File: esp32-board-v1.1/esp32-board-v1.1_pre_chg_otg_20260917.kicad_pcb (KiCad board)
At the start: 4 copper layers, 55 x 84 mm, 110 parts, among them J1 USB_C_Receptacle_GCT_USB4105-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, J2 X05B20U24T, J3 microSD_DM3AT-SF-PEJM5_EPDF, J4 Molex_PicoBlade_53261-0271_1x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, J5 Molex_PicoBlade_53261-0271_1x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, Q1 SOT-323_SC-70, SW1 SW_SPST_B3U-1000P, SW2 SW_SPST_B3U-1000P, SW3 SW_SPST_B3U-1000P, SW4 SW_SPST_B3U-1000P, SW5 SW_SPST_B3U-1000P, U1 ESP32-S3-WROOM-1_EPDF, U2 Texas_RTW_WQFN-24-1EP_4x4mm_P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, U3 RNM0015A, U4 TDFN-8-1EP_2x2mm_P0.5mm_EP0.8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, U5 Texas_X2QFN-12_1.6x1.6mm_P0.4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, U6 SOT-23-6

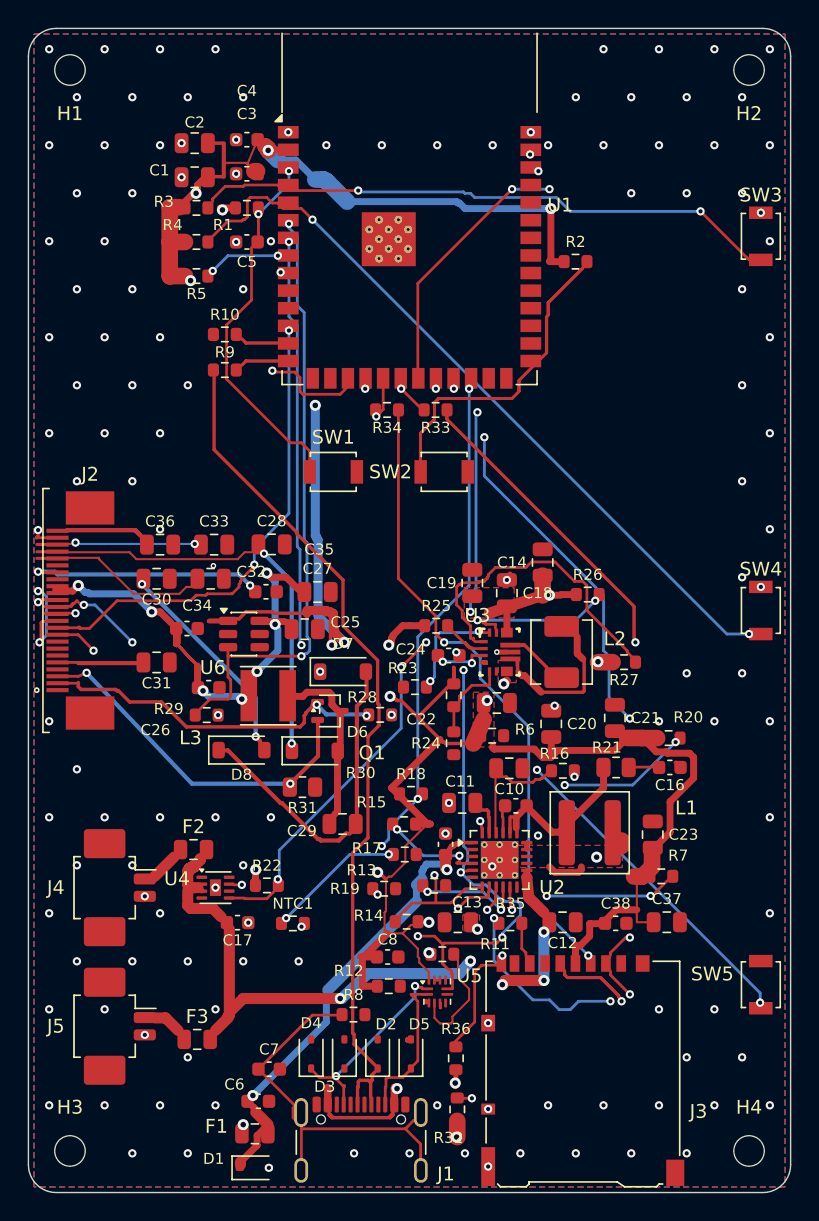
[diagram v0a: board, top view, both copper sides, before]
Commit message: 第四轮布线
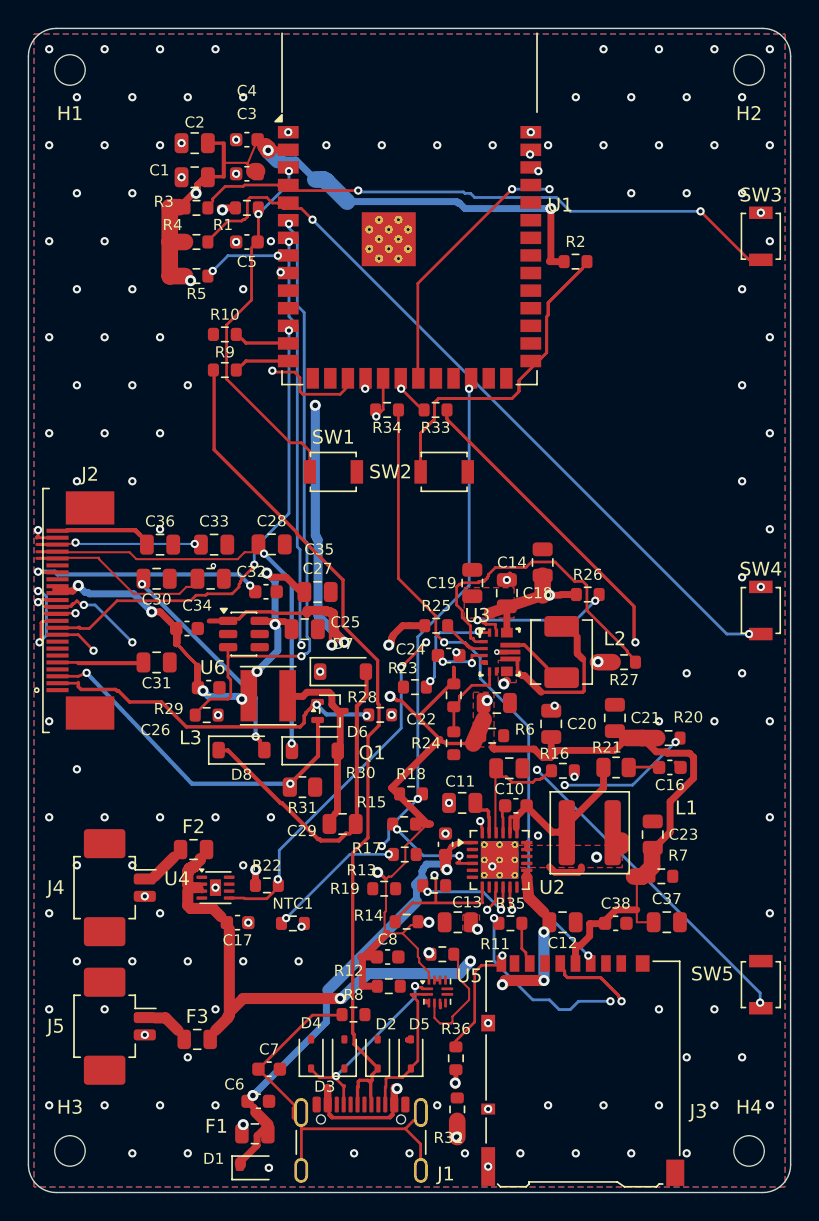
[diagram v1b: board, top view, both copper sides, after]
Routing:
- net I2C_SCL: track 83.3 -> 0.00 mm, vias 10 -> 0
- net TF_CS_N: track 65.4 -> 0.00 mm, vias 6 -> 0
- net CHG_OTG: track 9.09 -> 0.00 mm, vias 2 -> 0
- net CHG_INT_N: track 57.7 -> 58.4 mm
